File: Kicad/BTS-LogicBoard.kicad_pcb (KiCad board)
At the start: 2 copper layers, 54.6 x 55.9 mm, 49 parts, among them J1 Conn_01x06, J2 Conn_01x04, J3 Conn_01x02, Q1 BC817, Q2 BC807, Q3 BC817, Q4 BC807, Q5 BC817, SW1 SW_DPDT_x2, SW2 SW_DPDT_x2, U1 NCS2252SN2T1G, U2 NE555D, U3 NCS2252SN2T1G

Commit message: Started routing
Signed-off-by: Benoit Tarrade <btarrade@slb.com>
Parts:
- moved R13 18.6 mm to (127.0, 83.8), turned to 180 degrees
- moved Q3 16.0 mm to (125.7, 77.5), turned to 90 degrees
- moved Q4 14.8 mm to (132.1, 83.2)
- moved C1 14.0 mm to (142.2, 85.1)
- moved C4 14.0 mm to (142.2, 87.6)
- moved R15 14.0 mm to (139.1, 96.5), turned to 180 degrees
- moved R11 11.1 mm to (146.1, 92.7)
- moved R7 10.5 mm to (130.2, 78.1)
- moved Q2 9.16 mm to (138.4, 111.8)
- moved U3 9.09 mm to (139.1, 97.8)
- moved U1 3.18 mm to (139.1, 101.6), turned to 90 degrees
- moved C3 2.62 mm to (143.5, 106.0), turned to 270 degrees
- moved R2 0.45 mm to (146.1, 106.0)
- moved R10 0.15 mm to (141.0, 92.7)
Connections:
- C8 pad 1: GND -> Net-(C8-Pad1)
- C8 pad 2: Net-(C8-Pad2) -> GND
- Q4 pad 3: Net-(C8-Pad2) -> Net-(C8-Pad1)
- R14 pad 2: Net-(C8-Pad2) -> Net-(C8-Pad1)
- U3 pad 5: Net-(C8-Pad2) -> Net-(C8-Pad1)
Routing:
- net +5V: track 0.00 -> 75.4 mm, vias 0 -> 1
- net +12V: track 0.00 -> 18.6 mm, vias 0 -> 1
- net /2.5V: track 0.00 -> 15.8 mm, vias 0 -> 1
- net Net-(C8-Pad1): track 0.00 -> 11.7 mm, vias 0 -> 1
- net Net-(D2-Pad2): track 0.00 -> 10.9 mm
- net /VSense: track 0.00 -> 5.21 mm
- net /HIP_DISABLE: track 0.00 -> 4.19 mm, vias 0 -> 1
- net /PWM_Enabled_Line: track 0.00 -> 3.53 mm
- net /HIP_HEN: track 0.00 -> 3.35 mm
- net Net-(Q4-Pad1): track 0.00 -> 2.66 mm
- net Net-(C3-Pad2): track 0.00 -> 2.55 mm
- net Net-(Q3-Pad1): track 0.00 -> 2.10 mm
- net /Inv_Fan_trigger: track 0.00 -> 0.37 mm, vias 0 -> 1

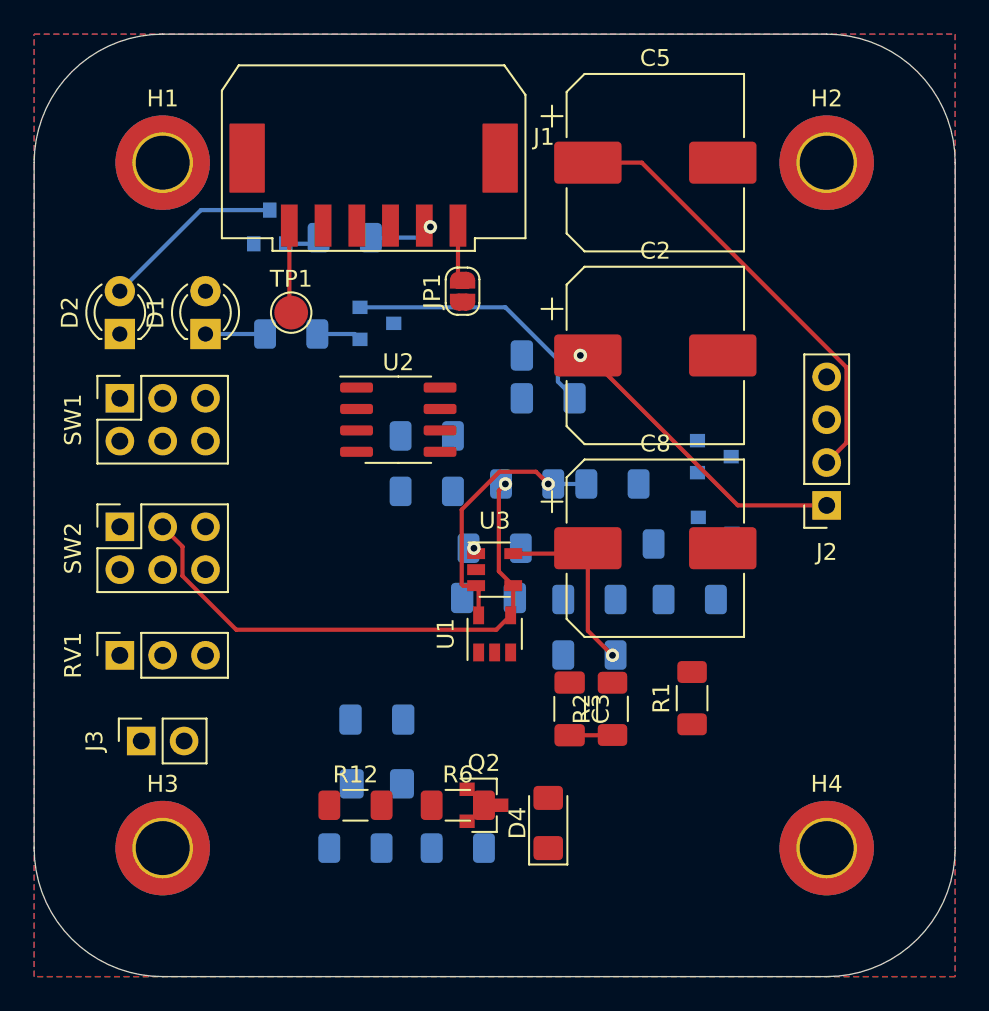
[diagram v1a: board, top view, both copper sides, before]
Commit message: Added NE555 enable override by HIP_DISABLE signal
Signed-off-by: Benoit Tarrade <btarrade@slb.com>
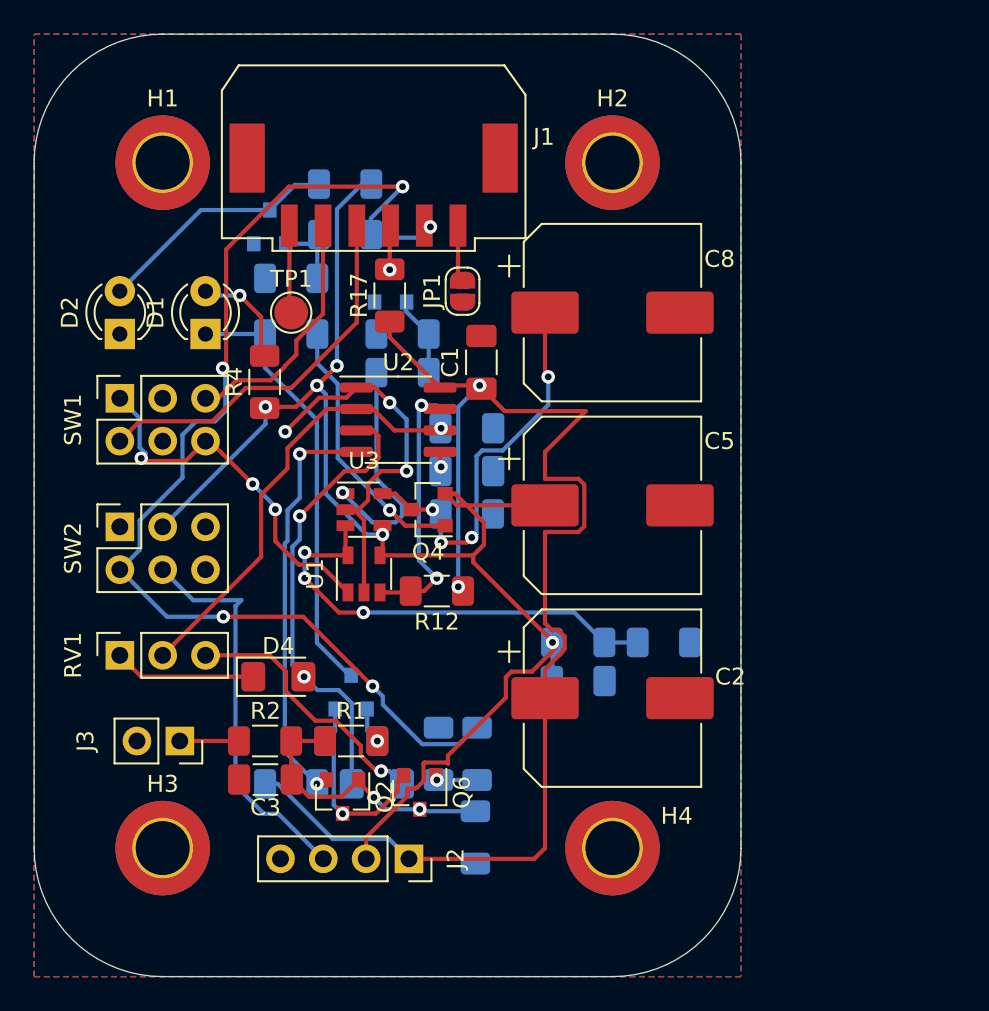
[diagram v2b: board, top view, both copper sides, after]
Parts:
- added Q6: BC817, Package_TO_SOT_SMD:SOT-23, F.Cu at (134.6, 111.0)
- added R18: 1k, Resistor_SMD:R_1206_3216Metric_Pad1.30x1.75mm_HandSolder, B.Cu at (138.0, 108.7)
- added R19: 56k, Resistor_SMD:R_1206_3216Metric_Pad1.30x1.75mm_HandSolder, B.Cu at (135.7, 108.7)
- C1, Q4, R17, R4: moved to F.Cu
- R2: value 56k -> 1k
- R5: value 1k -> 56k
- R6: moved to B.Cu
- moved R8 35.2 mm to (127.0, 80.5)
- moved J2 32.4 mm to (134.0, 114.9), turned to 270 degrees
- moved R9 32.0 mm to (130.2, 74.9), turned to 180 degrees
- moved R4 28.2 mm to (125.4, 86.7), turned to 90 degrees
- moved Q1 23.5 mm to (130.6, 105.1), turned to 90 degrees
- moved Q5 21.7 mm to (132.9, 80.9), turned to 90 degrees
- moved R17 21.6 mm to (132.8, 81.5), turned to 90 degrees
- moved R2 20.7 mm to (125.5, 108.0), turned to 180 degrees
- moved C5 20.5 mm to (146.1, 94.0)
- moved C2 20.5 mm to (146.1, 105.4)
- moved R1 20.4 mm to (130.6, 108.0), turned to 180 degrees
- moved R5 19.6 mm to (137.9, 113.7), turned to 270 degrees
- moved C3 18.5 mm to (125.5, 110.2), turned to 0 degrees
- moved D4 18.2 mm to (126.2, 104.1), turned to 0 degrees
- moved C4 16.9 mm to (144.0, 104.4), turned to 0 degrees
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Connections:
- net /PWM_Enabled_Line renamed /PWM_Enabled_INV
- net /SPY-line renamed /Pump-On
- C3 pad 2: Net-(C3-Pad2) -> /PWM_Enable
- Q2 pad 1: Net-(C3-Pad2) -> /PWM_Enable
- Q2 pad 2: /Reset-line -> Net-(Q2-Pad2)
- R1 pad 2: /Reset-line -> /PWM_Enable
- R2 pad 1: Net-(C3-Pad2) -> /PWM_Enable
- R5 pad 1: Net-(C3-Pad2) -> /PWM_Enable
- R6 pad 2: /Reset-line -> Net-(Q2-Pad2)
- U2 pad 4: /Reset-line -> Net-(Q2-Pad2)
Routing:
- net /HIP_DISABLE: track 4.19 -> 68.4 mm, vias 1 -> 5
- net +12V: track 18.6 -> 78.4 mm, vias 1 -> 2
- net GND: track 0.00 -> 34.4 mm, vias 0 -> 4
- net Net-(D3-Pad1): track 0.00 -> 27.1 mm, vias 0 -> 2
- net /Threshold: track 0.00 -> 25.9 mm, vias 0 -> 1
- net Net-(Q2-Pad2): track 0.00 -> 24.8 mm, vias 0 -> 2
- net /PSU_ON: track 0.00 -> 23.5 mm
- net /IN+: track 0.00 -> 22.7 mm
- net /PWM_Enabled_INV: track 3.53 -> 26.0 mm
- net /COMP-Out: track 0.00 -> 22.0 mm, vias 0 -> 3
- net /PWM_Enable: track 0.00 -> 16.9 mm, vias 0 -> 2
- net Net-(D3-Pad2): track 0.00 -> 15.8 mm, vias 0 -> 1
- net /NE-Out: track 0.00 -> 15.7 mm, vias 0 -> 2
- net /IN-: track 0.00 -> 14.8 mm
- net Net-(Q4-Pad1): track 2.66 -> 15.9 mm, vias 0 -> 1
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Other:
- board size 54.6 x 55.9 mm -> 41.9 x 55.9 mm
- rule trace_min: 0.2 -> 0

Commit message: Finalized board V1 and exported Gerber files
Signed-off-by: bebenlebricolo <benoittarrade@hotmail.fr>
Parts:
- added REF**: OSHW-Symbol_6.7x6mm_SilkScreen, Symbol:OSHW-Symbol_6.7x6mm_SilkScreen, F.Cu at (135.9, 105.4)
- added REF**: OSHW-Logo2_9.8x8mm_SilkScreen, Symbol:OSHW-Logo2_9.8x8mm_SilkScreen, B.Cu at (141.0, 81.9)
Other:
- board text added: "+12V"
- board text added: "+5V"
- board text added: "BTS-LogicBoard V1"
- board text added: "Designed by Benoit Tarrade (alias bebenlebricolo) https://github.com/bebenlebricolo"
- board text added: "GND"
- board text added: "PsuOn"
- board text added: "Pump"

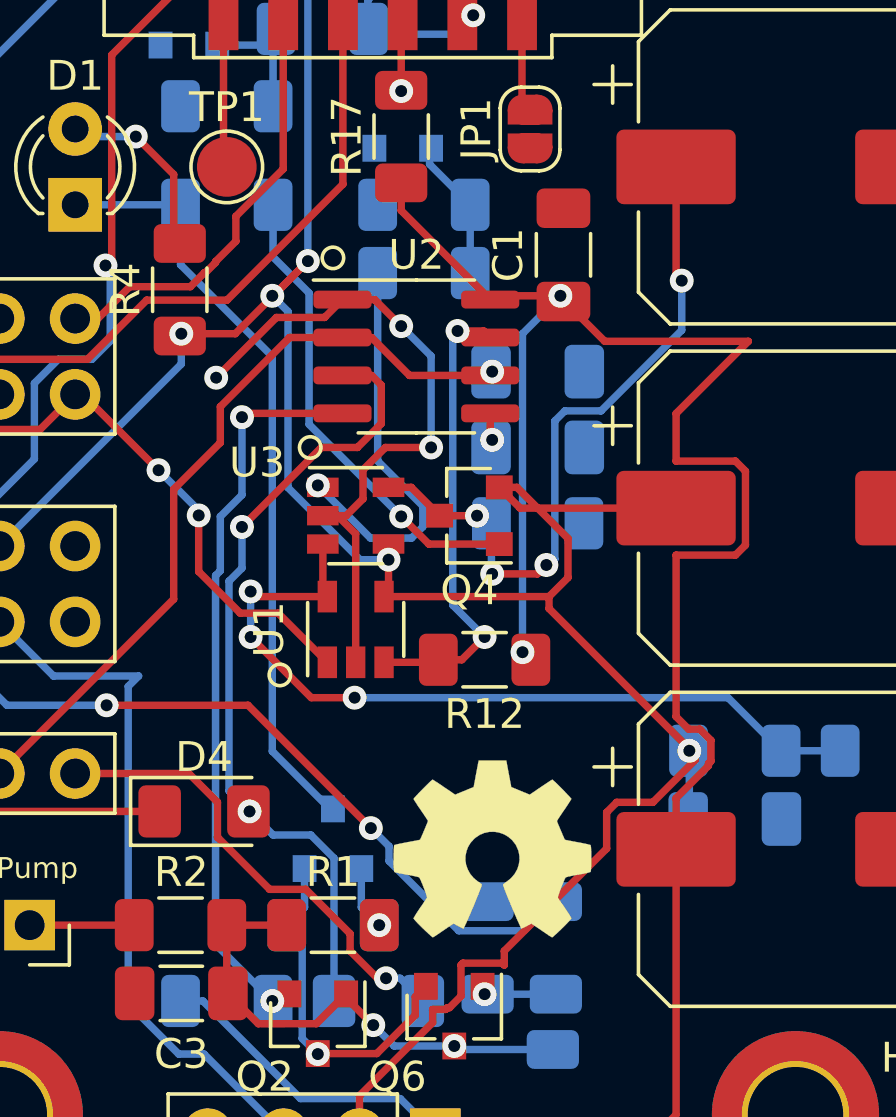
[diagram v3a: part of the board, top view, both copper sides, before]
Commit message: Fan trigger now uses 5V instead of 12v to prevent blowing up fans mosfets
Signed-off-by: bebenlebricolo <benoittarrade@hotmail.fr>
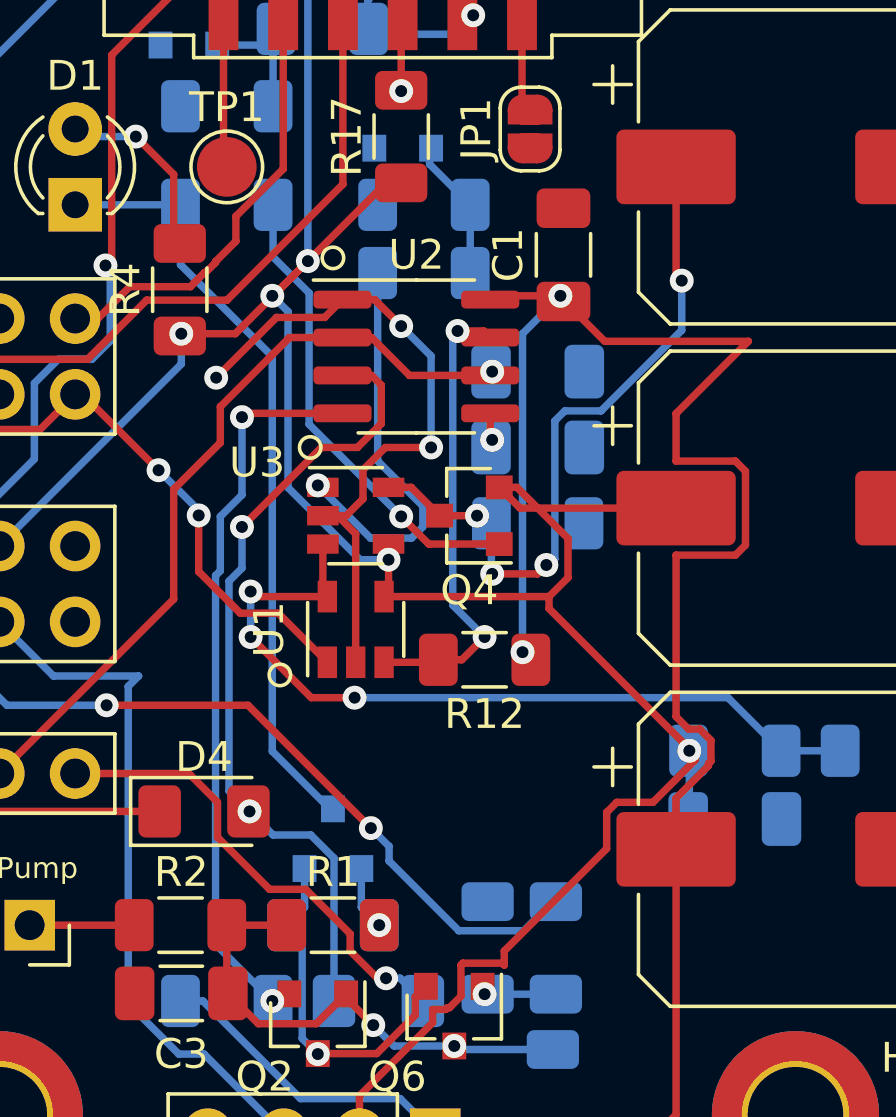
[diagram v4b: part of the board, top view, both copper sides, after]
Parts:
- removed REF**: OSHW-Symbol_6.7x6mm_SilkScreen, Symbol:OSHW-Symbol_6.7x6mm_SilkScreen
- removed REF**: OSHW-Logo2_9.8x8mm_SilkScreen, Symbol:OSHW-Logo2_9.8x8mm_SilkScreen
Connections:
- R17 pad 1: +12V -> +5V
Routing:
- net +12V: track 78.4 -> 73.2 mm
- net +5V: track 88.0 -> 92.2 mm
